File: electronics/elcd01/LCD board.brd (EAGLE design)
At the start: 129.2 x 39.4 mm, 5 parts, among them SW1 ENCODER_SW1-PEC12, X1 HD44780LCD-1602

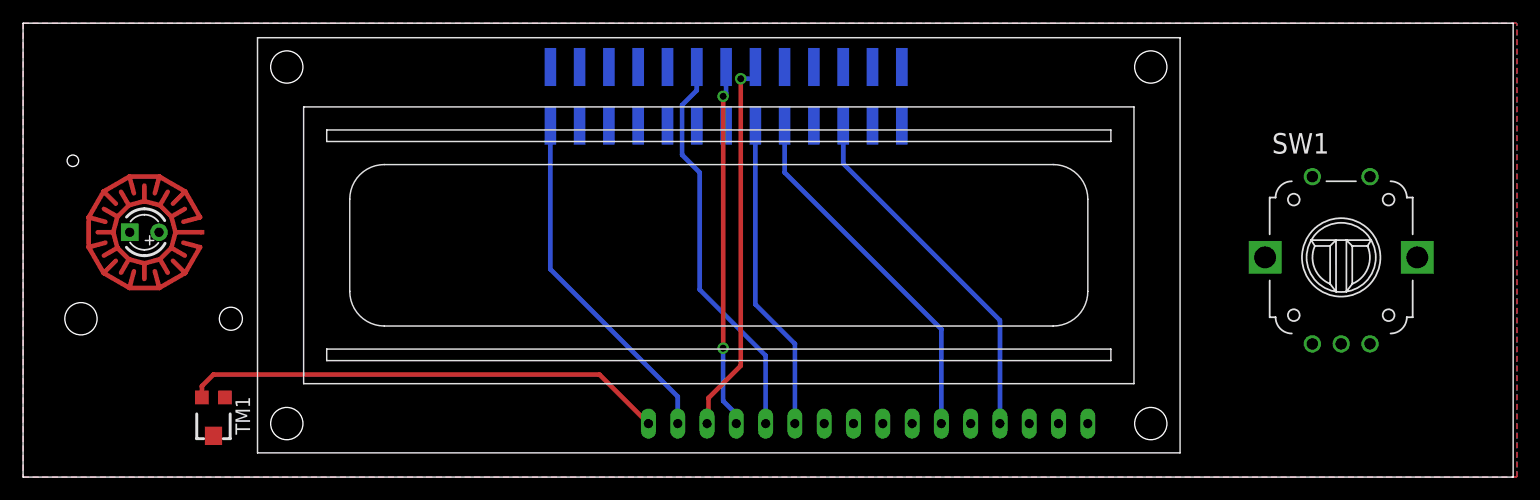
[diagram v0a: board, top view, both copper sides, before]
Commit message: Changed connector on LCD board.  Added notes to EMC01 board.
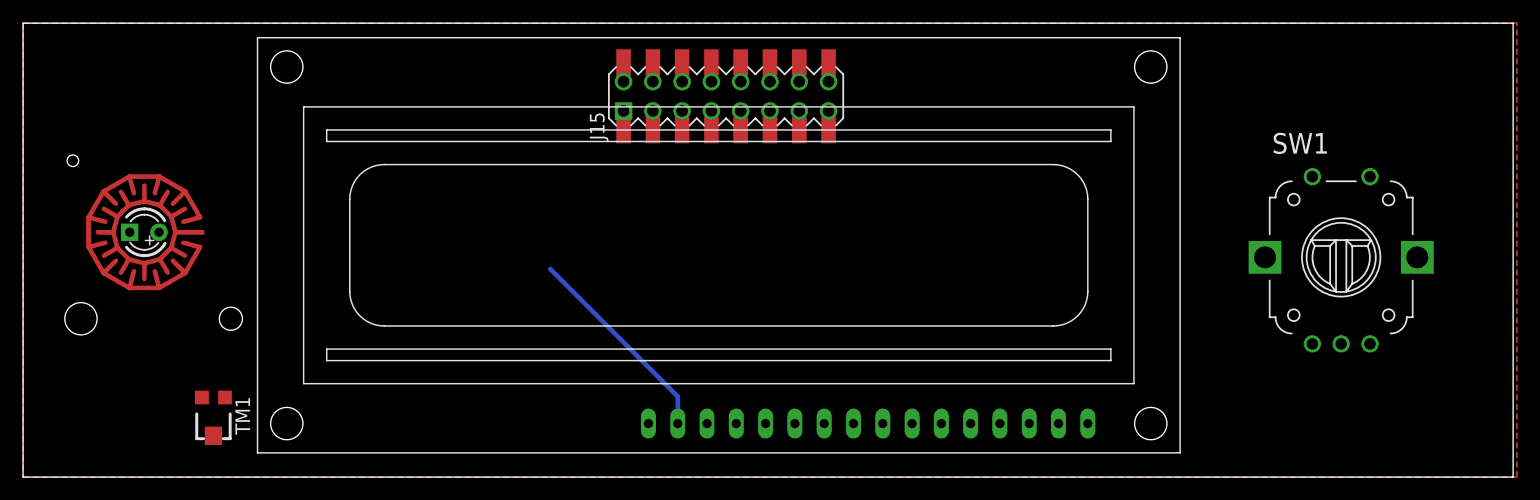
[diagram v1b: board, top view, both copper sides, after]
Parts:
- removed JP1: (no value), pinhead-2:2X13SMD
- added J15: CONN-RECT-16PIN-2ROW, FirePick:CONN-RECT-2.54MM-16PIN-2ROW-SMTH
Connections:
- removed net +3V3: JP1.1
- removed net N$2: JP1.16, X1.11
- removed net N$3: JP1.22, X1.4
- removed net N$4: JP1.11, X1.12
- removed net N$5: JP1.13, X1.13
- removed net N$6: JP1.18, X1.6
- removed net N$7: JP1.15, X1.14
- new net +3V3_RASPI: J15.2
- new net LCD_/E: J15.7, X1.6
- new net LCD_DB4: J15.9, X1.11
- new net LCD_DB5: J15.10, X1.12
- new net LCD_DB6: J15.11, X1.13
- new net LCD_DB7: J15.12, X1.14
- new net LCD_RS: J15.8, X1.4
- new net PANEL_ENC_A: J15.5
- new net PANEL_ENC_B: J15.6
- new net PANEL_ENC_SW: J15.4
- new net PANEL_LED_GRN: J15.13
- new net PANEL_LED_RED: J15.14
- new net PANEL_PUSHBTN: J15.15
- net +5V: now also J15.1, TM1.3; no longer JP1.2, TM1.1
- net GND: now also J15.16, J15.3, TM1.1; no longer JP1.6, TM1.3
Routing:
- net GND: track 41.9 -> 0.00 mm
- net N$4: track 34.4 -> 0.00 mm
- net N$7: track 33.5 -> 0.00 mm, vias 1 -> 0
- net N$5: track 31.5 -> 0.00 mm, vias 2 -> 0
- net N$6: track 31.5 -> 0.00 mm
- net N$3: track 31.5 -> 0.00 mm
- net N$2: track 27.3 -> 0.00 mm
- net +5V: track 30.4 -> 18.0 mm
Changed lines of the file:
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@@
 <layer number="111" name="LPC17xx" color="7" fill="1" visible="yes" active="yes"/>
 <layer number="112" name="tSilk" color="7" fill="1" visible="yes" active="yes"/>
+<layer number="113" name="IDFDebug" color="4" fill="1" visible="yes" active="yes"/>
 <layer number="116" name="Patch_BOT" color="9" fill="4" visible="yes" active="yes"/>
 <layer number="121" name="_tsilk" color="7" fill="1" visible="yes" active="yes"/>
@@
 <classes>
 <class number="0" name="default" width="0" drill="0">
+</class>
+<class number="1" name="power" width="0" drill="0">
 </class>
 </classes>
@@
 <elements>
 <element name="X1" library="adafruit" package="LCD1602" value="HD44780LCD-1602" x="90.17" y="38.1" rot="R180"/>
-<element name="JP1" library="pinhead-2" package="2X13SMD" value="" x="36.83" y="31.75" rot="MR180"/>
 <element name="TM1" library="adafruit" package="TC33X" value="" x="6.35" y="5.08" smashed="yes" rot="R180">
 <attribute name="NAME" x="8.255" y="6.985" size="1.27" layer="25" rot="R270"/>
@@
 <element name="LED1" library="Adafruit Trellis" package="ELAST_PAD_SQUARE_10MM_5.4MM_4X4GRID" value="" x="7.62" y="13.97"/>
 <element name="SW1" library="dp_devices" package="PEC12_INCREMENTAL_ENCODER" value="ENCODER_SW1-PEC12" x="104.14" y="19.05"/>
+<element name="J15" library="FirePick" package="CONN-RECT-2.54MM-16PIN-2ROW-SMTH" value="CONN-RECT-16PIN-2ROW" x="50.8" y="33.02"/>
 </elements>
 <signals>
 <signal name="GND">
-<contactref element="X1" pad="1"/>
-<contactref element="TM1" pad="3"/>
-<contactref element="X1" pad="16"/>
-<contactref element="JP1" pad="6"/>
-<contactref element="X1" pad="5"/>
 <polygon width="0.4064" layer="16">
 <vertex x="-10.16" y="39.37"/>
@@
 <vertex x="119.38" y="39.37"/>
 </polygon>
-<wire x1="5.35" y1="6.905" x2="5.35" y2="7.89" width="0.4064" layer="1"/>
-<wire x1="5.35" y1="7.89" x2="6.35" y2="8.89" width="0.4064" layer="1"/>
-<wire x1="6.35" y1="8.89" x2="39.82" y2="8.89" width="0.4064" layer="1"/>
-<wire x1="39.82" y1="8.89" x2="44.07" y2="4.64" width="0.4064" layer="1"/>
+<contactref element="J15" pad="16"/>
+<contactref element="J15" pad="3"/>
+<contactref element="TM1" pad="1"/>
+<contactref element="X1" pad="1"/>
+<contactref element="X1" pad="5"/>
+<contactref element="X1" pad="16"/>
+<wire x1="44.45" y1="31.75" x2="59.69" y2="34.29" width="0" layer="19" extent="1-1"/>
+<wire x1="44.07" y1="4.64" x2="44.45" y2="31.75" width="0" layer="19" extent="1-1"/>
+<wire x1="72.01" y1="4.64" x2="44.07" y2="4.64" width="0" layer="19" extent="1-1"/>
+<wire x1="82.17" y1="4.64" x2="72.01" y2="4.64" width="0" layer="19" extent="1-1"/>
+<wire x1="7.35" y1="6.905" x2="44.07" y2="4.64" width="0" layer="19" extent="1-1"/>
 </signal>
 <signal name="+5V">
-<contactref element="TM1" pad="1"/>
-<contactref element="JP1" pad="2"/>
-<contactref element="X1" pad="15"/>
 <polygon width="0.4064" layer="1">
 <vertex x="-10.16" y="39.37"/>
@@
 <vertex x="119.38" y="39.37"/>
 </polygon>
+<contactref element="J15" pad="1"/>
+<contactref element="TM1" pad="3"/>
+<contactref element="X1" pad="15"/>
 <wire x1="46.61" y1="4.64" x2="46.61" y2="6.984" width="0.4064" layer="16"/>
 <wire x1="46.61" y1="6.984" x2="35.56" y2="18.034" width="0.4064" layer="16"/>
-<wire x1="35.56" y1="18.034" x2="35.56" y2="30.48" width="0.4064" layer="16"/>
+<wire x1="35.56" y1="18.034" x2="41.91" y2="31.75" width="0" layer="19" extent="16-16"/>
+<wire x1="5.35" y1="6.905" x2="35.56" y2="18.034" width="0" layer="19" extent="1-16"/>
 </signal>
 <signal name="N$1">
 <contactref element="TM1" pad="2"/>
 </signal>
-<signal name="N$3">
+<signal name="+3V3_RASPI">
+<contactref element="J15" pad="2"/>
+</signal>
+<signal name="LCD_DB5">
+<contactref element="J15" pad="10"/>
+<contactref element="X1" pad="12"/>
+<wire x1="54.23" y1="4.64" x2="52.07" y2="34.29" width="0" layer="19" extent="1-1"/>
+</signal>
+<signal name="LCD_DB6">
+<contactref element="J15" pad="11"/>
+<contactref element="X1" pad="13"/>
+<wire x1="51.69" y1="4.64" x2="54.61" y2="31.75" width="0" layer="19" extent="1-1"/>
+</signal>
+<signal name="PANEL_LED_GRN">
+<contactref element="J15" pad="13"/>
+</signal>
+<signal name="PANEL_ENC_B">
+<contactref element="J15" pad="6"/>
+</signal>
+<signal name="PANEL_PUSHBTN">
+<contactref element="J15" pad="15"/>
+</signal>
+<signal name="PANEL_LED_RED">
+<contactref element="J15" pad="14"/>
+</signal>
+<signal name="LCD_DB4">
+<contactref element="J15" pad="9"/>
+<contactref element="X1" pad="11"/>
+<wire x1="56.77" y1="4.64" x2="52.07" y2="31.75" width="0" layer="19" extent="1-1"/>
+</signal>
+<signal name="LCD_/E">
+<contactref element="J15" pad="7"/>
+<contactref element="X1" pad="6"/>
+<wire x1="69.47" y1="4.64" x2="49.53" y2="31.75" width="0" layer="19" extent="1-1"/>
+</signal>
+<signal name="LCD_RS">
+<contactref element="J15" pad="8"/>
 <contactref element="X1" pad="4"/>
-<contactref element="JP1" pad="22"/>
-<wire x1="74.55" y1="4.64" x2="74.55" y2="13.588" width="0.4064" layer="16"/>
-<wire x1="74.55" y1="13.588" x2="60.96" y2="27.178" width="0.4064" layer="16"/>
-<wire x1="60.96" y1="27.178" x2="60.96" y2="30.48" width="0.4064" layer="16"/>
-</signal>
-<signal name="N$6">
-<contactref element="X1" pad="6"/>
-<contactref element="JP1" pad="18"/>
-<wire x1="69.47" y1="4.64" x2="69.47" y2="12.826" width="0.4064" layer="16"/>
-<wire x1="69.47" y1="12.826" x2="55.88" y2="26.416" width="0.4064" layer="16"/>
-<wire x1="55.88" y1="26.416" x2="55.88" y2="30.48" width="0.4064" layer="16"/>
-</signal>
-<signal name="N$2">
-<contactref element="X1" pad="11"/>
-<contactref element="JP1" pad="16"/>
-<wire x1="56.77" y1="4.64" x2="56.77" y2="11.556" width="0.4064" layer="16"/>
-<wire x1="56.77" y1="11.556" x2="53.34" y2="14.986" width="0.4064" layer="16"/>
-<wire x1="53.34" y1="14.986" x2="53.34" y2="30.48" width="0.4064" layer="16"/>
-</signal>
-<signal name="N$4">
-<contactref element="X1" pad="12"/>
-<contactref element="JP1" pad="11"/>
-<wire x1="54.23" y1="4.64" x2="54.23" y2="10.54" width="0.4064" layer="16"/>
-<wire x1="54.23" y1="10.54" x2="48.514" y2="16.256" width="0.4064" layer="16"/>
-<wire x1="48.514" y1="16.256" x2="48.514" y2="26.416" width="0.4064" layer="16"/>
-<wire x1="48.514" y1="26.416" x2="46.99" y2="27.94" width="0.4064" layer="16"/>
-<wire x1="46.99" y1="27.94" x2="46.99" y2="32.258" width="0.4064" layer="16"/>
-<wire x1="46.99" y1="32.258" x2="48.26" y2="33.528" width="0.4064" layer="16"/>
-<wire x1="48.26" y1="33.528" x2="48.26" y2="35.56" width="0.4064" layer="16"/>
-</signal>
-<signal name="N$5">
-<contactref element="X1" pad="13"/>
-<contactref element="JP1" pad="13"/>
-<wire x1="51.562" y1="5.588" x2="51.562" y2="4.826" width="0.4064" layer="16"/>
-<wire x1="50.546" y1="6.604" x2="51.562" y2="5.588" width="0.4064" layer="16"/>
-<wire x1="50.546" y1="11.176" x2="50.546" y2="6.604" width="0.4064" layer="16"/>
-<wire x1="50.546" y1="33.02" x2="50.546" y2="11.176" width="0.4064" layer="1"/>
-<wire x1="50.8" y1="33.274" x2="50.546" y2="33.02" width="0.4064" layer="16"/>
-<wire x1="50.8" y1="35.56" x2="50.8" y2="33.274" width="0.4064" layer="16"/>
-<wire x1="51.562" y1="4.826" x2="51.69" y2="4.64" width="0.4064" layer="16"/>
-<via x="50.546" y="11.176" extent="1-16" drill="0.6"/>
-<via x="50.546" y="33.02" extent="1-16" drill="0.6"/>
-</signal>
-<signal name="N$7">
+<wire x1="74.55" y1="4.64" x2="49.53" y2="34.29" width="0" layer="19" extent="1-1"/>
+</signal>
+<signal name="PANEL_ENC_SW">
+<contactref element="J15" pad="4"/>
+</signal>
+<signal name="PANEL_ENC_A">
+<contactref element="J15" pad="5"/>
+</signal>
+<signal name="LCD_DB7">
+<contactref element="J15" pad="12"/>
 <contactref element="X1" pad="14"/>
-<contactref element="JP1" pad="15"/>
-<wire x1="52.07" y1="34.544" x2="52.07" y2="9.652" width="0.4064" layer="1"/>
-<wire x1="53.086" y1="34.544" x2="52.07" y2="34.544" width="0.4064" layer="16"/>
-<wire x1="53.34" y1="34.798" x2="53.086" y2="34.544" width="0.4064" layer="16"/>
-<wire x1="53.34" y1="35.56" x2="53.34" y2="34.798" width="0.4064" layer="16"/>
-<via x="52.07" y="34.544" extent="1-16" drill="0.6"/>
-<wire x1="49.276" y1="4.826" x2="49.15" y2="4.64" width="0.4064" layer="1"/>
-<wire x1="52.07" y1="9.652" x2="49.276" y2="6.858" width="0.4064" layer="1"/>
-<wire x1="49.276" y1="6.858" x2="49.276" y2="4.766" width="0.4064" layer="1"/>
-<wire x1="49.276" y1="4.766" x2="49.15" y2="4.64" width="0.4064" layer="1"/>
-</signal>
-<signal name="+3V3">
-<contactref element="JP1" pad="1"/>
+<wire x1="49.15" y1="4.64" x2="54.61" y2="34.29" width="0" layer="19" extent="1-1"/>
+</signal>
+<signal name="N$8">
 </signal>
 </signals>

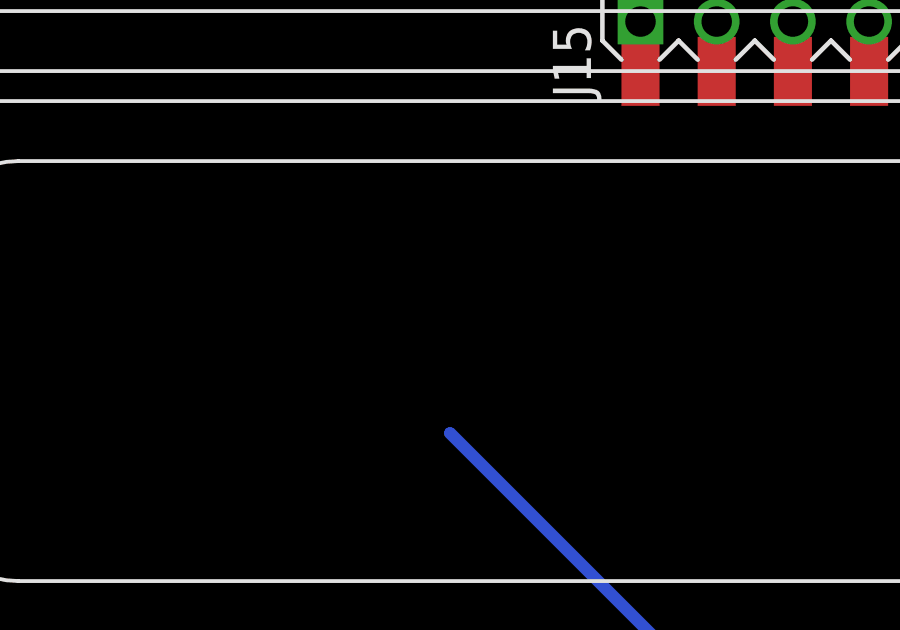
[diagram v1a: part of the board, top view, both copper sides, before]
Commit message: Wired up encoder, switches, and LEDs
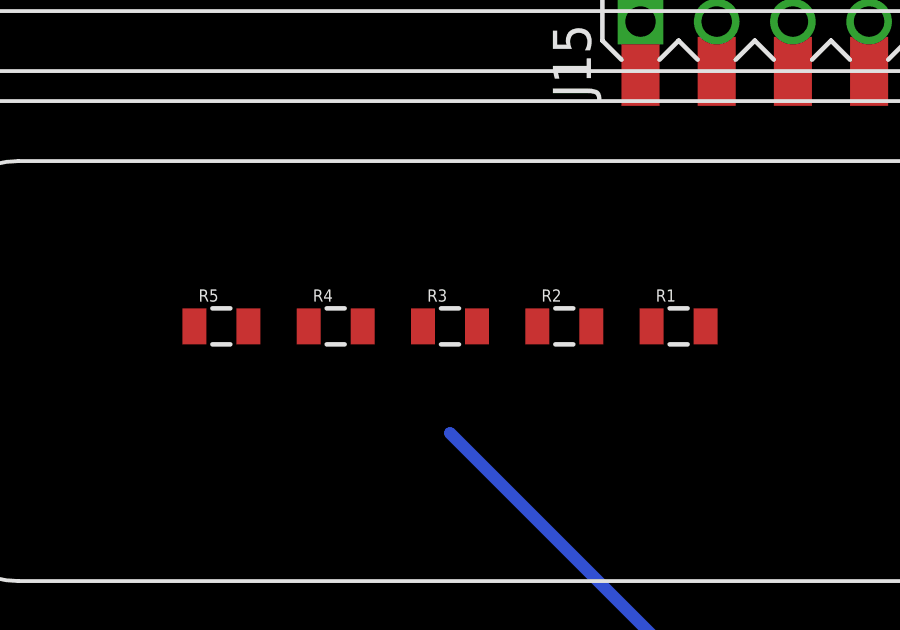
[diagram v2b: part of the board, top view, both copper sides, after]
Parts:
- added R1: 55, SparkFun-Passives:0805
- added R2, R3, R4, R5: 10K, SparkFun-Passives:0805
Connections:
- removed net +3V3_RASPI: J15.2
- new net 3.3V: J15.2, R2.2, R3.2, R4.2, R5.2
- new net N$2: LED1.K, R1.2
- net +5V: now also X1.2
- net GND: now also LED1.SW1, SW1.C, SW1.P2
- net N$1: now also X1.3
- net PANEL_ENC_A: now also R3.1, SW1.A
- net PANEL_ENC_B: now also R4.1, SW1.B
- net PANEL_ENC_SW: now also R5.1, SW1.P1
- net PANEL_LED_GRN: now also LED1.A1
- net PANEL_LED_RED: now also R1.1
- net PANEL_PUSHBTN: now also LED1.SW2, R2.1
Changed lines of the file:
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@@
 <element name="SW1" library="dp_devices" package="PEC12_INCREMENTAL_ENCODER" value="ENCODER_SW1-PEC12" x="104.14" y="19.05"/>
 <element name="J15" library="FirePick" package="CONN-RECT-2.54MM-16PIN-2ROW-SMTH" value="CONN-RECT-16PIN-2ROW" x="50.8" y="33.02"/>
+<element name="R1" library="SparkFun-Passives" package="0805" value="55" x="43.18" y="21.59"/>
+<element name="R2" library="SparkFun-Passives" package="0805" value="10K" x="39.37" y="21.59"/>
+<element name="R3" library="SparkFun-Passives" package="0805" value="10K" x="35.56" y="21.59"/>
+<element name="R4" library="SparkFun-Passives" package="0805" value="10K" x="31.75" y="21.59"/>
+<element name="R5" library="SparkFun-Passives" package="0805" value="10K" x="27.94" y="21.59"/>
 </elements>
 <signals>
@@
 <contactref element="X1" pad="5"/>
 <contactref element="X1" pad="16"/>
-<wire x1="44.45" y1="31.75" x2="59.69" y2="34.29" width="0" layer="19" extent="1-1"/>
-<wire x1="44.07" y1="4.64" x2="44.45" y2="31.75" width="0" layer="19" extent="1-1"/>
-<wire x1="72.01" y1="4.64" x2="44.07" y2="4.64" width="0" layer="19" extent="1-1"/>
-<wire x1="82.17" y1="4.64" x2="72.01" y2="4.64" width="0" layer="19" extent="1-1"/>
+<contactref element="LED1" pad="SW1"/>
+<contactref element="SW1" pad="C"/>
+<contactref element="SW1" pad="P2"/>
+<wire x1="104.14" y1="11.55" x2="106.64" y2="26.05" width="0" layer="19" extent="1-1"/>
+<wire x1="82.17" y1="4.64" x2="104.14" y2="11.55" width="0" layer="19" extent="1-1"/>
+<wire x1="72.01" y1="4.64" x2="82.17" y2="4.64" width="0" layer="19" extent="1-1"/>
+<wire x1="44.07" y1="4.64" x2="72.01" y2="4.64" width="0" layer="19" extent="1-1"/>
+<wire x1="44.45" y1="31.75" x2="44.07" y2="4.64" width="0" layer="19" extent="1-1"/>
+<wire x1="59.69" y1="34.29" x2="44.45" y2="31.75" width="0" layer="19" extent="1-1"/>
 <wire x1="7.35" y1="6.905" x2="44.07" y2="4.64" width="0" layer="19" extent="1-1"/>
+<wire x1="5.36" y1="21.23" x2="7.35" y2="6.905" width="0" layer="19" extent="1-1"/>
 </signal>
 <signal name="+5V">
@@
 <wire x1="46.61" y1="4.64" x2="46.61" y2="6.984" width="0.4064" layer="16"/>
 <wire x1="46.61" y1="6.984" x2="35.56" y2="18.034" width="0.4064" layer="16"/>
-<wire x1="35.56" y1="18.034" x2="41.91" y2="31.75" width="0" layer="19" extent="16-16"/>
+<contactref element="X1" pad="2"/>
+<wire x1="46.61" y1="4.64" x2="79.63" y2="4.64" width="0" layer="19" extent="1-1"/>
+<wire x1="41.91" y1="31.75" x2="35.56" y2="18.034" width="0" layer="19" extent="16-16"/>
 <wire x1="5.35" y1="6.905" x2="35.56" y2="18.034" width="0" layer="19" extent="1-16"/>
 </signal>
 <signal name="N$1">
 <contactref element="TM1" pad="2"/>
-</signal>
-<signal name="+3V3_RASPI">
-<contactref element="J15" pad="2"/>
+<contactref element="X1" pad="3"/>
+<wire x1="6.35" y1="3.58" x2="77.09" y2="4.64" width="0" layer="19" extent="1-1"/>
 </signal>
 <signal name="LCD_DB5">
@@
 <signal name="PANEL_LED_GRN">
 <contactref element="J15" pad="13"/>
+<contactref element="LED1" pad="A1"/>
+<wire x1="1.63" y1="21.23" x2="57.15" y2="31.75" width="0" layer="19" extent="1-1"/>
 </signal>
 <signal name="PANEL_ENC_B">
 <contactref element="J15" pad="6"/>
+<contactref element="R4" pad="1"/>
+<contactref element="SW1" pad="B"/>
+<wire x1="46.99" y1="34.29" x2="106.64" y2="11.55" width="0" layer="19" extent="1-1"/>
+<wire x1="30.85" y1="21.59" x2="46.99" y2="34.29" width="0" layer="19" extent="1-1"/>
 </signal>
 <signal name="PANEL_PUSHBTN">
 <contactref element="J15" pad="15"/>
+<contactref element="LED1" pad="SW2"/>
+<contactref element="R2" pad="1"/>
+<wire x1="-4.47" y1="21.22" x2="59.69" y2="31.75" width="0" layer="19" extent="1-1"/>
+<wire x1="38.47" y1="21.59" x2="-4.47" y2="21.22" width="0" layer="19" extent="1-1"/>
 </signal>
 <signal name="PANEL_LED_RED">
 <contactref element="J15" pad="14"/>
+<contactref element="R1" pad="1"/>
+<wire x1="42.28" y1="21.59" x2="57.15" y2="34.29" width="0" layer="19" extent="1-1"/>
 </signal>
 <signal name="LCD_DB4">
@@
 <signal name="PANEL_ENC_SW">
 <contactref element="J15" pad="4"/>
+<contactref element="R5" pad="1"/>
+<contactref element="SW1" pad="P1"/>
+<wire x1="44.45" y1="34.29" x2="101.64" y2="26.05" width="0" layer="19" extent="1-1"/>
+<wire x1="27.04" y1="21.59" x2="44.45" y2="34.29" width="0" layer="19" extent="1-1"/>
 </signal>
 <signal name="PANEL_ENC_A">
 <contactref element="J15" pad="5"/>
+<contactref element="R3" pad="1"/>
+<contactref element="SW1" pad="A"/>
+<wire x1="46.99" y1="31.75" x2="101.64" y2="11.55" width="0" layer="19" extent="1-1"/>
+<wire x1="34.66" y1="21.59" x2="46.99" y2="31.75" width="0" layer="19" extent="1-1"/>
 </signal>
 <signal name="LCD_DB7">
@@
 <wire x1="49.15" y1="4.64" x2="54.61" y2="34.29" width="0" layer="19" extent="1-1"/>
 </signal>
-<signal name="N$8">
+<signal name="CONTRAST">
+</signal>
+<signal name="N$2">
+<contactref element="R1" pad="2"/>
+<contactref element="LED1" pad="K"/>
+<wire x1="-0.91" y1="21.23" x2="44.08" y2="21.59" width="0" layer="19" extent="1-1"/>
+</signal>
+<signal name="3.3V">
+<contactref element="J15" pad="2"/>
+<contactref element="R3" pad="2"/>
+<contactref element="R5" pad="2"/>
+<contactref element="R4" pad="2"/>
+<contactref element="R2" pad="2"/>
+<wire x1="40.27" y1="21.59" x2="41.91" y2="34.29" width="0" layer="19" extent="1-1"/>
+<wire x1="36.46" y1="21.59" x2="40.27" y2="21.59" width="0" layer="19" extent="1-1"/>
+<wire x1="32.65" y1="21.59" x2="36.46" y2="21.59" width="0" layer="19" extent="1-1"/>
+<wire x1="28.84" y1="21.59" x2="32.65" y2="21.59" width="0" layer="19" extent="1-1"/>
 </signal>
 </signals>
